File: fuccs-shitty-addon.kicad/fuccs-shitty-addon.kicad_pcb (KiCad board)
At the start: 2 copper layers, 50.2 x 44.5 mm, 3 parts

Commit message: Rotate connector pinout to make it more obvious which pins are the SA pins. Label tracks, tidy up schematic, and point the LED footprints at a local footprint lib
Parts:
- removed the G*** at (0.94, -22.5) (x3)
- added G*** (x3): LOGO, LOGO, F.Cu at (0.94, -22.5)
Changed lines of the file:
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@@
     (37 F.SilkS user)
     (38 B.Mask user)
-    (39 F.Mask user)
+    (39 F.Mask user hide)
     (40 Dwgs.User user)
     (41 Cmts.User user)
@@
     (solder_mask_min_width 0.25)
     (aux_axis_origin 0 0)
-    (visible_elements FFFFFF7F)
+    (visible_elements FEFFFF7F)
     (pcbplotparams
       (layerselection 0x010f0_80000001)

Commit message: Components placed
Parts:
- removed the G*** at (0.94, -22.5) (x3)
- added C1: 100nF, Capacitors_SMD:C_0805_HandSoldering, B.Cu at (71.3, -16.3)
- added D1: LED L, fuccs-shitty-addon-footprints:LED_TOPLED-Reverse-Gullwing_Handsoldering, B.Cu at (-6.60, -19.0)
- added D2: LED R, fuccs-shitty-addon-footprints:LED_TOPLED-Reverse-Gullwing_Handsoldering, B.Cu at (6.60, -19.0)
- added G*** (x3): LOGO, LOGO, F.Cu at (0.94, -22.5)
- added J1: Shitty Addon + ISP, Pin_Headers:Pin_Header_Straight_2x03_Pitch2.54mm_SMD, B.Cu at (-1.27, -7.38)
- added R1: 10K, Resistors_SMD:R_0805_HandSoldering, B.Cu at (76.7, -15.8)
- added R2: 100, Resistors_SMD:R_0805_HandSoldering, B.Cu at (-9.44, -21.8)
- added R3: 100, Resistors_SMD:R_0805_HandSoldering, B.Cu at (9.44, -21.8)
- added U1: ATtiny85-20SU, Housings_SOIC:SOIJ-8_5.3x5.3mm_Pitch1.27mm, B.Cu at (0.00, -27.0)
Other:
- board size 50.2 x 44.5 mm -> 135.4 x 50.2 mm
- net class Default: via_dia 0.6 -> 0.8
- rule pad_to_mask_clearance: 0.2 -> 0.051

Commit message: Routing complete
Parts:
- removed the G*** at (0.94, -22.5) (x3)
- added G*** (x2), GND: LOGO, LOGO, F.Cu at (0.94, -22.5)
- J1: footprint Pin_Headers:Pin_Header_Straight_2x03_Pitch2.54mm_SMD -> fuccs-shitty-addon-footprints:Pin_Header_Straight_2x03_Pitch2.54mm_SMD_no-silk
- U1: value ATtiny85-20SU -> ATtiny85-20SUR
- moved R1 77.0 mm to (-0.11, -22.0), turned to 0 degrees
- moved C1 71.3 mm to (0.00, -16.0)
- moved U1 1.00 mm to (0.00, -28.0)
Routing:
- net /SCL_SCK: track 0.00 -> 51.5 mm
- net /MISO: track 0.00 -> 41.2 mm
- net /SDA_MOSI: track 0.00 -> 35.1 mm
- net /~RESET~: track 0.00 -> 33.1 mm
- net +3V3: track 0.00 -> 29.5 mm
- net /LED_R: track 0.00 -> 15.2 mm
- net /LED_L: track 0.00 -> 8.09 mm
- net Net-(D2-Pad1): track 0.00 -> 4.51 mm
- net Net-(D1-Pad1): track 0.00 -> 4.51 mm
- added copper zone on B.Cu, net (none)
- added copper zone on B.Cu, net GND
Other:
- board size 135.4 x 50.2 mm -> 50.2 x 44.5 mm
- net class Default: trace_width 0.25 -> 0.4
- board text added: "3V3"
- board text added: "ATtiny85-20SU"
- board text added: "GND"
- board text added: "SCL"
- board text added: "SDA"
- board text added: "Shitty connections"

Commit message: Fix layer alignment and weird artefacts miles outside the board perimeter
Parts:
- removed the G*** at (0.94, -22.5) (x2)
- removed GND: LOGO, LOGO
- added G*** (x3): LOGO, LOGO, F.Cu at (0.94, -22.5)
- added G***: LOGO, LOGO, F.Cu at (0.70, -22.7)
- added G***: LOGO, LOGO, F.Cu at (111.6, -30.7)
- added G***: LOGO, LOGO, F.Cu at (52.3, -30.8)
- added G***: LOGO, LOGO, F.Cu at (96.3, -31.8)
- added G***: LOGO, LOGO, F.Cu at (75.3, -30.8)
- added G***: LOGO, LOGO, F.Cu at (55.3, -27.8)
- added G***: LOGO, LOGO, F.Cu at (57.3, -24.8)
- added G***: LOGO, LOGO, F.Cu at (112.5, -29.8)
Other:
- net class Default: trace_width 0.4 -> 0.25; via_dia 0.8 -> 0.6
- rule pad_to_mask_clearance: 0.051 -> 0.2
- board text added: "@jannf"
- board text added: "@jeffmakes"
- board text added: "●⊚●●●⊚●⊚ ●⊚●⊚●●⊚● ●⊚●●⊚⊚⊚● ●⊚●⊚●⊚⊚⊚"

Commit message: Gerbers released for production
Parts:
- removed the G*** at (0.94, -22.5) (x3)
- added G*** (x3): LOGO, LOGO, F.Cu at (0.94, -22.5)
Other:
- rule pad_to_mask_clearance: 0.2 -> 0
- rule solder_mask_min_width: 0.25 -> 0.1
- board text added: "rev1 2019"
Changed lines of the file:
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@@
   (general
     (thickness 1.6)
-    (drawings 43)
+    (drawings 44)
     (tracks 63)
     (zones 0)
-    (modules 52)
+    (modules 19)
     (nets 11)
   )
@@
   )
   (layers
-    (0 F.Cu signal)
+    (0 F.Cu signal hide)
     (31 B.Cu signal hide)
     (32 B.Adhes user hide)
     (33 F.Adhes user hide)
-    (34 B.Paste user hide)
-    (35 F.Paste user)
-    (36 B.SilkS user hide)
-    (37 F.SilkS user)
-    (38 B.Mask user hide)
-    (39 F.Mask user)
+    (34 B.Paste user)
+    (35 F.Paste user hide)
+    (36 B.SilkS user)
+    (37 F.SilkS user hide)
+    (38 B.Mask user)
+    (39 F.Mask user hide)
     (40 Dwgs.User user hide)
     (41 Cmts.User user hide)
@@
     (44 Edge.Cuts user)
     (45 Margin user hide)
-    (46 B.CrtYd user hide)
-    (47 F.CrtYd user)
+    (46 B.CrtYd user)
+    (47 F.CrtYd user hide)
     (48 B.Fab user hide)
-    (49 F.Fab user)
+    (49 F.Fab user hide)
   )
   (setup
@@
     (pad_size 1.524 1.524)
     (pad_drill 0.762)
-    (pad_to_mask_clearance 0.2)
-    (solder_mask_min_width 0.25)
+    (pad_to_mask_clearance 0)
+    (solder_mask_min_width 0.1)
     (aux_axis_origin 0 0)
     (visible_elements FEFFFFFF)
     (pcbplotparams
-      (layerselection 0x010f0_80000001)
+      (layerselection 0x010f0_ffffffff)
       (usegerberextensions false)
       (usegerberattributes false)
@@
       (outputformat 1)
       (mirror false)
-      (drillshape 1)
+      (drillshape 0)
       (scaleselection 1)
-      (outputdirectory "gerbers/"))
+      (outputdirectory "../gerber/"))
   )
   (net 0 "")
@@
     )
   )
+  (gr_text "rev1 2019" (at 11.7 -7.9 24) (layer B.SilkS)
+    (effects (font (size 1.2 1.2) (thickness 0.2)) (justify mirror))
+  )
+  (gr_text "●⊚●●●⊚●⊚\n●⊚●⊚●●⊚●\n●⊚●●⊚⊚⊚●\n●⊚●⊚●⊚⊚⊚\n" (at -12.199777 -29.35003 180) (layer B.SilkS)
+    (effects (font (size 1 1) (thickness 0.1)) (justify mirror))
+  )
   (gr_line (start -22.564212 -44.49385) (end -12.591695 -37.92164) (layer Edge.Cuts) (width 0.1))
   (gr_line (start -12.591695 -37.92164) (end -0.787248 -32.714733) (layer Edge.Cuts) (width 0.1))
@@
   (gr_line (start -22.273352 -25.429423) (end -25.079902 -42.56636) (layer Edge.Cuts) (width 0.1))
   (gr_line (start -25.079902 -42.56636) (end -22.564212 -44.49385) (layer Edge.Cuts) (width 0.1))
-  (gr_text "●⊚●●●⊚●⊚\n●⊚●⊚●●⊚●\n●⊚●●⊚⊚⊚●\n●⊚●⊚●⊚⊚⊚\n" (at -12.199777 -29.35003 180) (layer B.SilkS)
-    (effects (font (size 1 1) (thickness 0.1)) (justify mirror))
-  )
   (gr_text " @jannf\n" (at -13.399777 -6.20003 -26) (layer B.Mask)
     (effects (font (size 1.2 1.2) (thickness 0.2)) (justify mirror))

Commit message: Add FUCCS handle to bottom silk
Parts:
- removed the G*** at (0.94, -22.5) (x3)
- added G*** (x3): LOGO, LOGO, F.Cu at (0.94, -22.5)
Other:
- board text added: "@FUCSScurity"
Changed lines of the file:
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@@
   (general
     (thickness 1.6)
-    (drawings 44)
+    (drawings 45)
     (tracks 63)
     (zones 0)
@@
     (pad 6 smd rect (at 2.525 -2.54 270) (size 3.15 1) (layers B.Cu B.Paste B.Mask)
       (net 5 /SCL_SCK))
-    (model ${KISYS3DMOD}/Pin_Headers.3dshapes/Pin_Header_Straight_2x03_Pitch2.54mm_SMD.wrl
+    (model ${KISYS3DMOD}/Connector_PinHeader_2.54mm.3dshapes/PinHeader_2x03_P2.54mm_Vertical_SMD.step
       (at (xyz 0 0 0))
       (scale (xyz 1 1 1))
@@
     (pad 2 smd rect (at 1.35 0) (size 1.5 1.3) (layers B.Cu B.Paste B.Mask)
       (net 7 /~RESET~))
-    (model ${KISYS3DMOD}/Resistors_SMD.3dshapes/R_0805.wrl
+    (model ${KISYS3DMOD}/Resistor_SMD.3dshapes/R_0805_2012Metric.wrl
       (at (xyz 0 0 0))
       (scale (xyz 1 1 1))
@@
     (pad 2 smd rect (at 1.35 0 45) (size 1.5 1.3) (layers B.Cu B.Paste B.Mask)
       (net 9 /LED_L))
-    (model ${KISYS3DMOD}/Resistors_SMD.3dshapes/R_0805.wrl
+    (model ${KISYS3DMOD}/Resistor_SMD.3dshapes/R_0805_2012Metric.wrl
       (at (xyz 0 0 0))
       (scale (xyz 1 1 1))
@@
     (pad 2 smd rect (at 1.35 0 135) (size 1.5 1.3) (layers B.Cu B.Paste B.Mask)
       (net 10 /LED_R))
-    (model ${KISYS3DMOD}/Resistors_SMD.3dshapes/R_0805.wrl
+    (model ${KISYS3DMOD}/Resistor_SMD.3dshapes/R_0805_2012Metric.wrl
       (at (xyz 0 0 0))
       (scale (xyz 1 1 1))
@@
     (pad 1 smd rect (at -3.65 1.905) (size 1.7 0.65) (layers B.Cu B.Paste B.Mask)
       (net 7 /~RESET~))
-    (model ${KISYS3DMOD}/Housings_SOIC.3dshapes/SOIJ-8_5.3x5.3mm_Pitch1.27mm.wrl
+    (model ${KISYS3DMOD}/Package_SO.3dshapes/SOIJ-8_5.3x5.3mm_P1.27mm.wrl
       (at (xyz 0 0 0))
       (scale (xyz 1 1 1))
@@
     (pad 1 smd rect (at -2.54 0 135) (size 2 2.6) (layers B.Cu B.Paste B.Mask)
       (net 4 "Net-(D2-Pad1)"))
-    (model ${KISYS3DMOD}/LEDs.3dshapes/LED_PLCC-2.wrl
+    (model ${KISYS3DMOD}/LEDs.3dshapes/LED_SMD.3dshapes/LED_1210_3225Metric.step
       (at (xyz 0 0 0))
       (scale (xyz 1 1 1))
@@
     )
   )
+  (gr_text @FUCSScurity (at -11.9 -7.6 -26) (layer B.SilkS)
+    (effects (font (size 1.2 1.15) (thickness 0.2)) (justify mirror))
+  )
   (gr_text "rev1 2019" (at 11.7 -7.9 24) (layer B.SilkS)

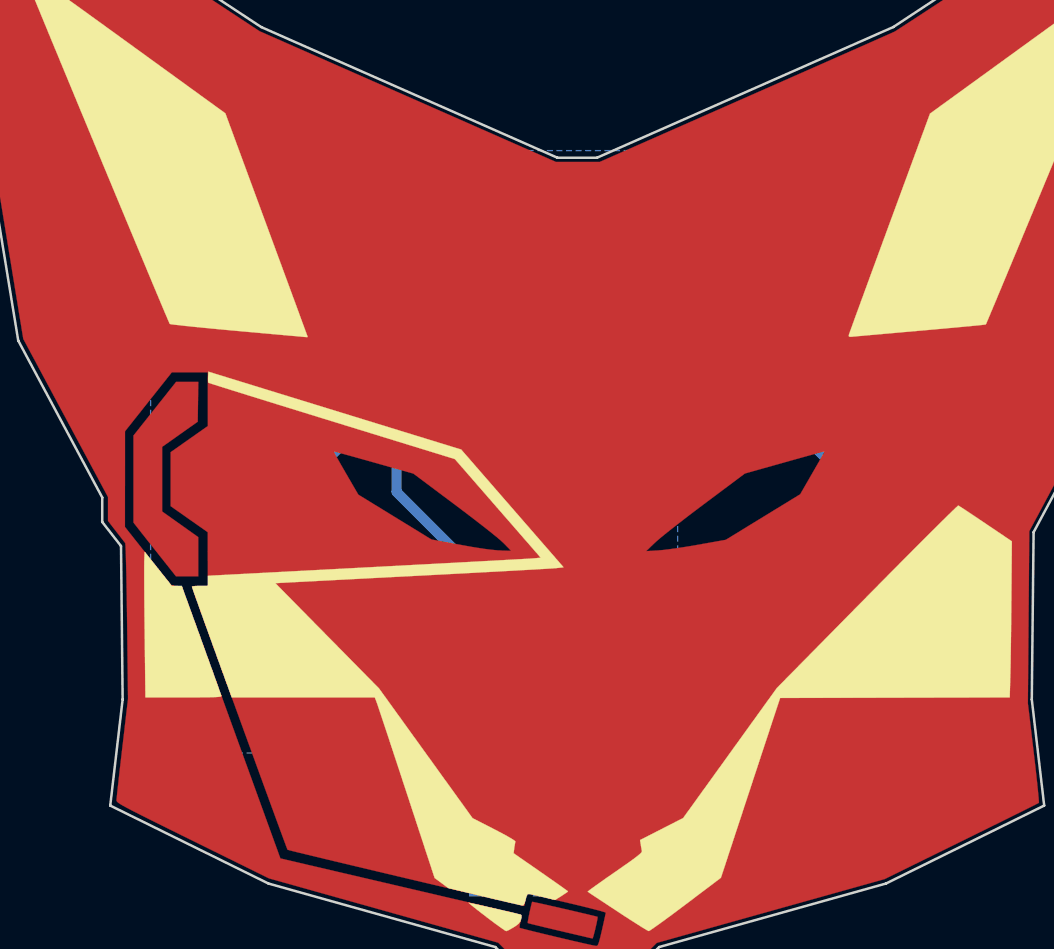
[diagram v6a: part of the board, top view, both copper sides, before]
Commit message: Reroute track out of keepout region. Add keepouts. Add pin labels for the MISO and RESET signals, bump revision number
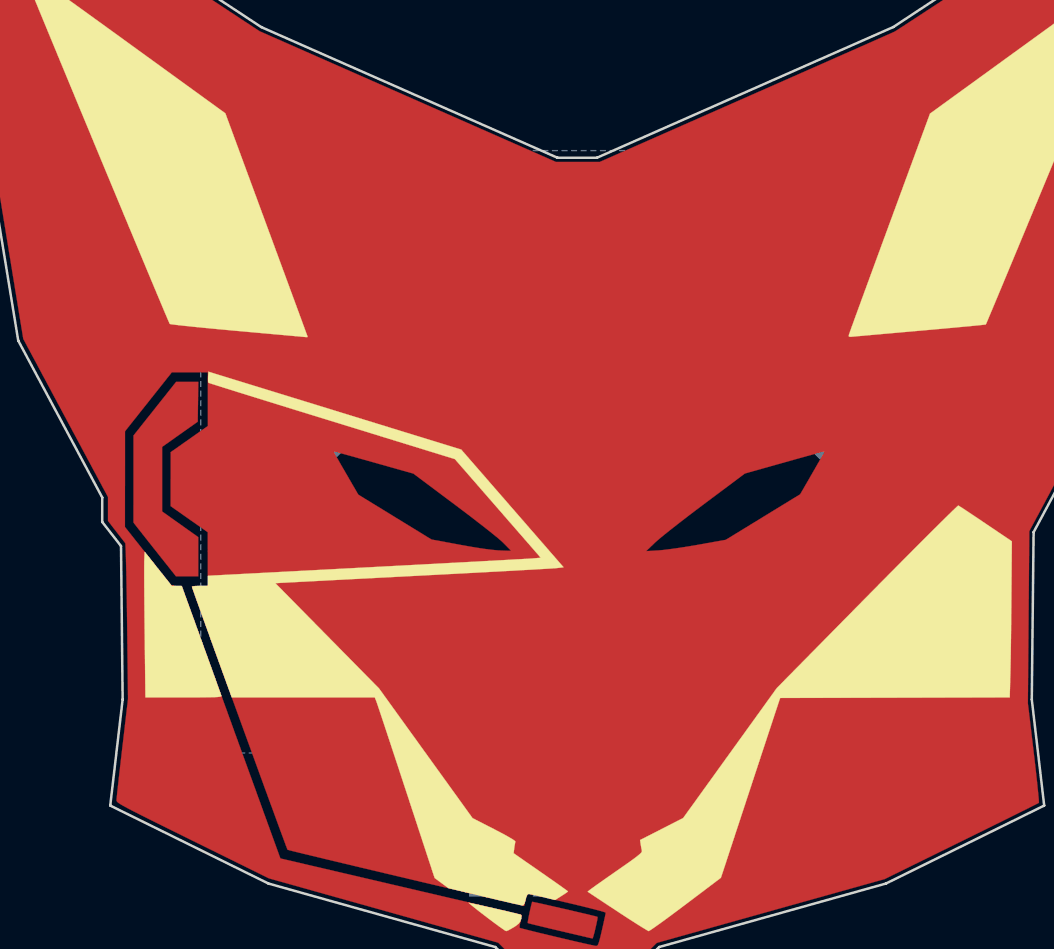
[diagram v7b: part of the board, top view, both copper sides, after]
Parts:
- removed the G*** at (0.94, -22.5) (x3)
- added G*** (x3): LOGO, LOGO, F.Cu at (0.94, -22.5)
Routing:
- net /~RESET~: track 33.1 -> 44.4 mm
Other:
- board text added: "MISO"
- board text added: "rev2 2019"
- board text added: "~RESET~"
- board text removed: "rev1 2019"

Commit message: Mask windows under LED's
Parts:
- removed the G*** at (0.94, -22.5) (x3)
- added G*** (x3): LOGO, LOGO, F.Cu at (0.94, -22.5)
